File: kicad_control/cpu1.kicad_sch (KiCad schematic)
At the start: 12 parts, among them J1 backplane 2, J2 backplane 1, U1 W27C512-45Z, U10 74LS139, U2 W27C512-45Z, U3 W27C512-45Z, U4 W27C512-45Z, U5 74S151, U6 74LS374, U7 74LS374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

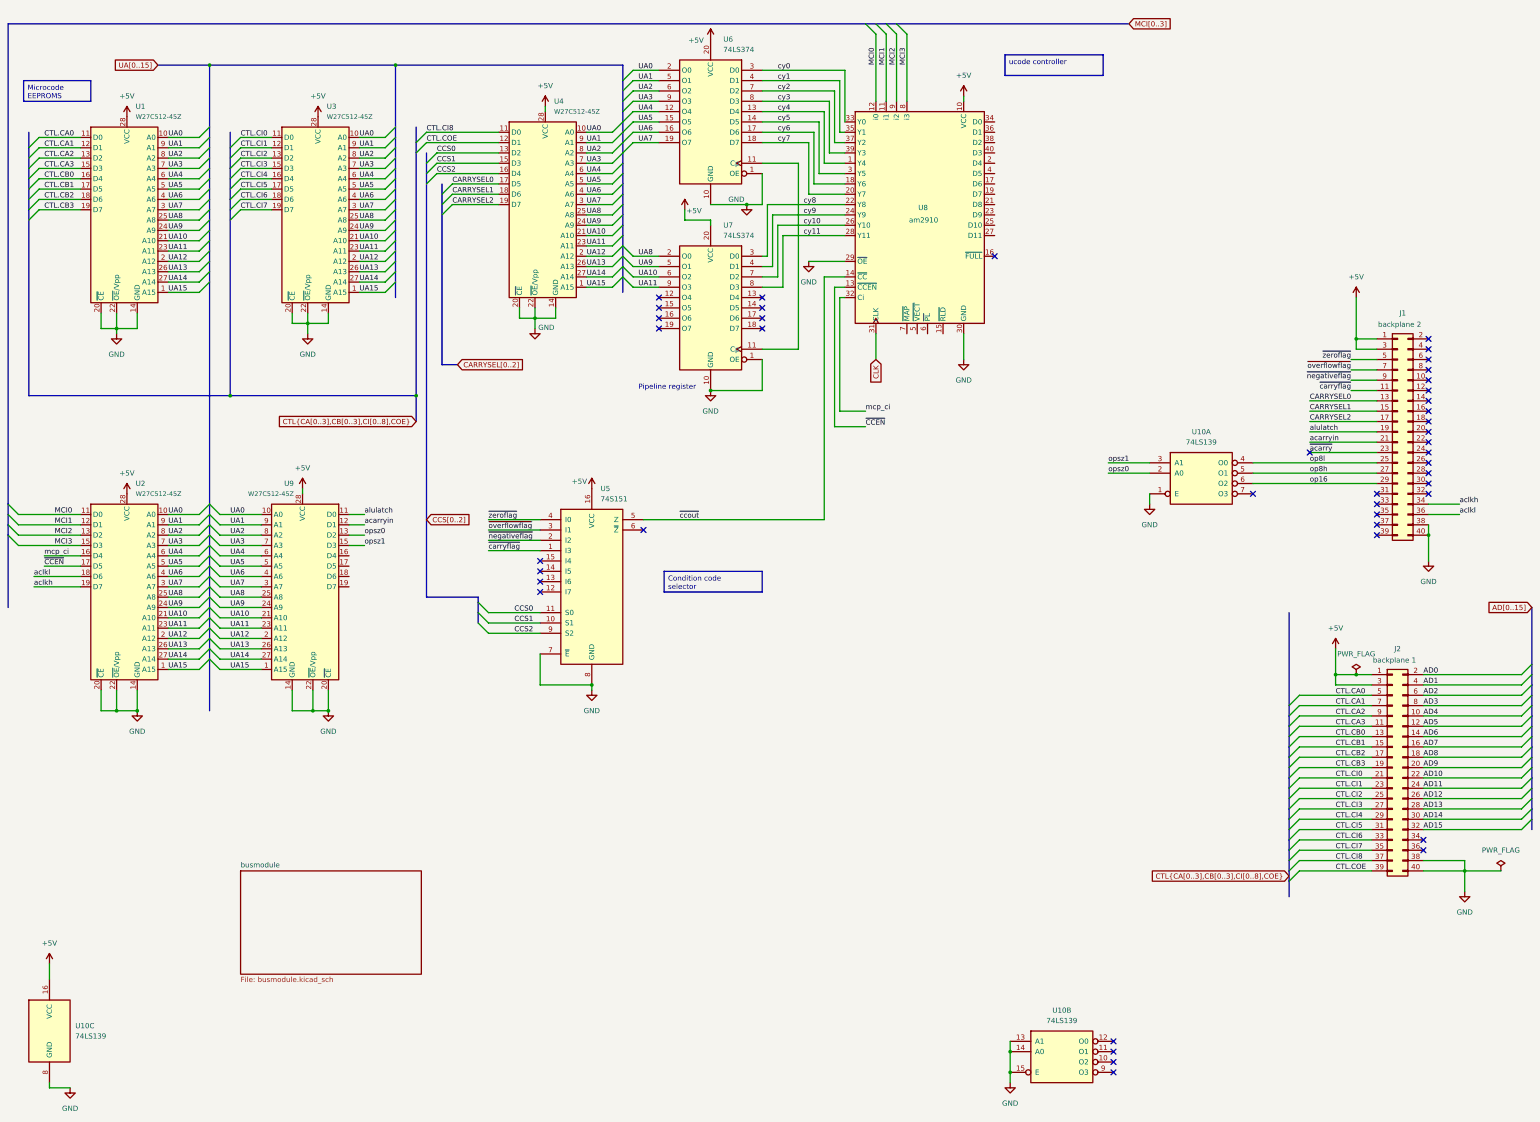
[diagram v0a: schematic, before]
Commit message: Redoing control board because of pipeline blunder. This also is the last version with the distinct program counter.
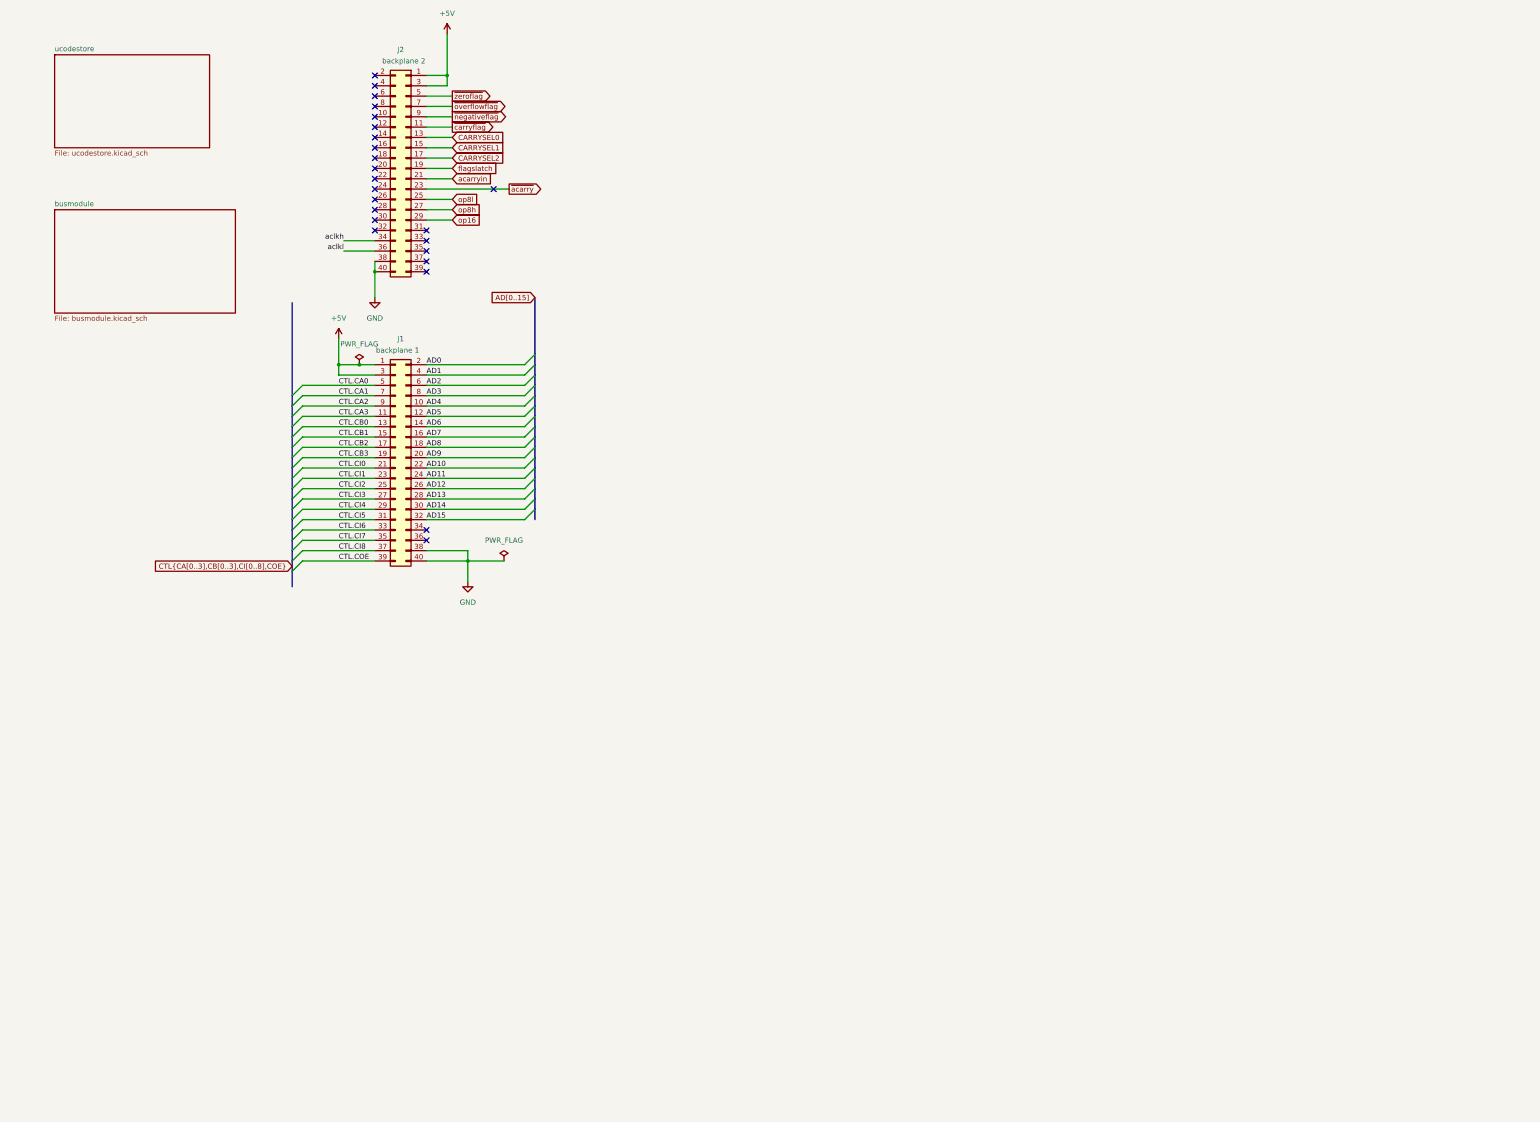
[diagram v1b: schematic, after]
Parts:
- removed U1, U2, U3, U4, U9: W27C512-45Z, Package_DIP:DIP-28_W15.24mm, symbol frits:W27C512-45Z
- removed U10: 74LS139, symbol 74xx:74LS139
- removed U5: 74S151, symbol 74xx:74LS151
- removed U6, U7: 74LS374, symbol 74xx:74LS374
- removed U8: am2910, Package_DIP:DIP-40_W15.24mm, symbol frits:am2910
- renumbered J2 to J1, J1 to J2
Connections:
- net alulatch renamed flagslatch
- no-connect marks 43 -> 24
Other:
- added sheet ucodestore (ucodestore.kicad_sch)
- note removed: "Pipeline register"
- company: ErrorSort -> ErrorSoft
- moved on the sheet: J1, J2
